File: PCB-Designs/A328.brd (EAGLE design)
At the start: 35.2 x 39.4 mm, 15 parts

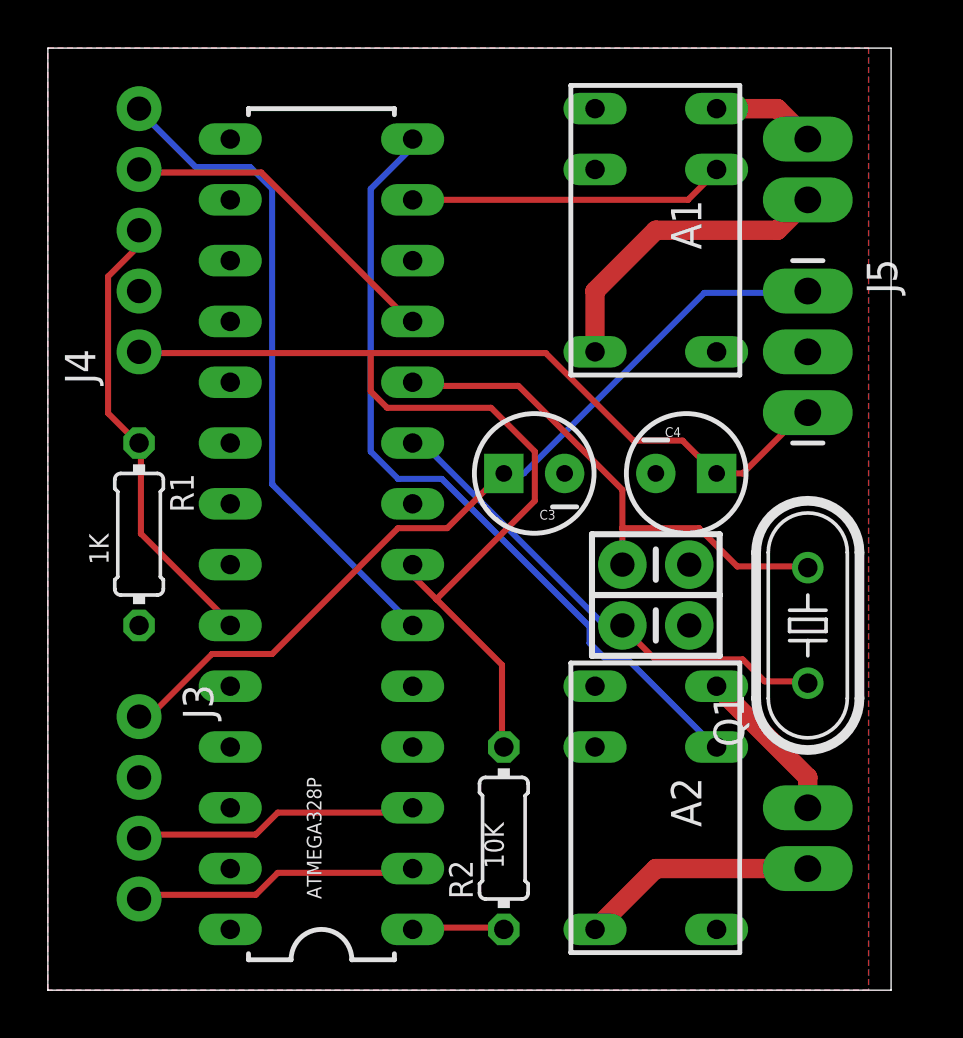
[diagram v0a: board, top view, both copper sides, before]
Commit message: Smaller board, redundant power according to arduino schematic.
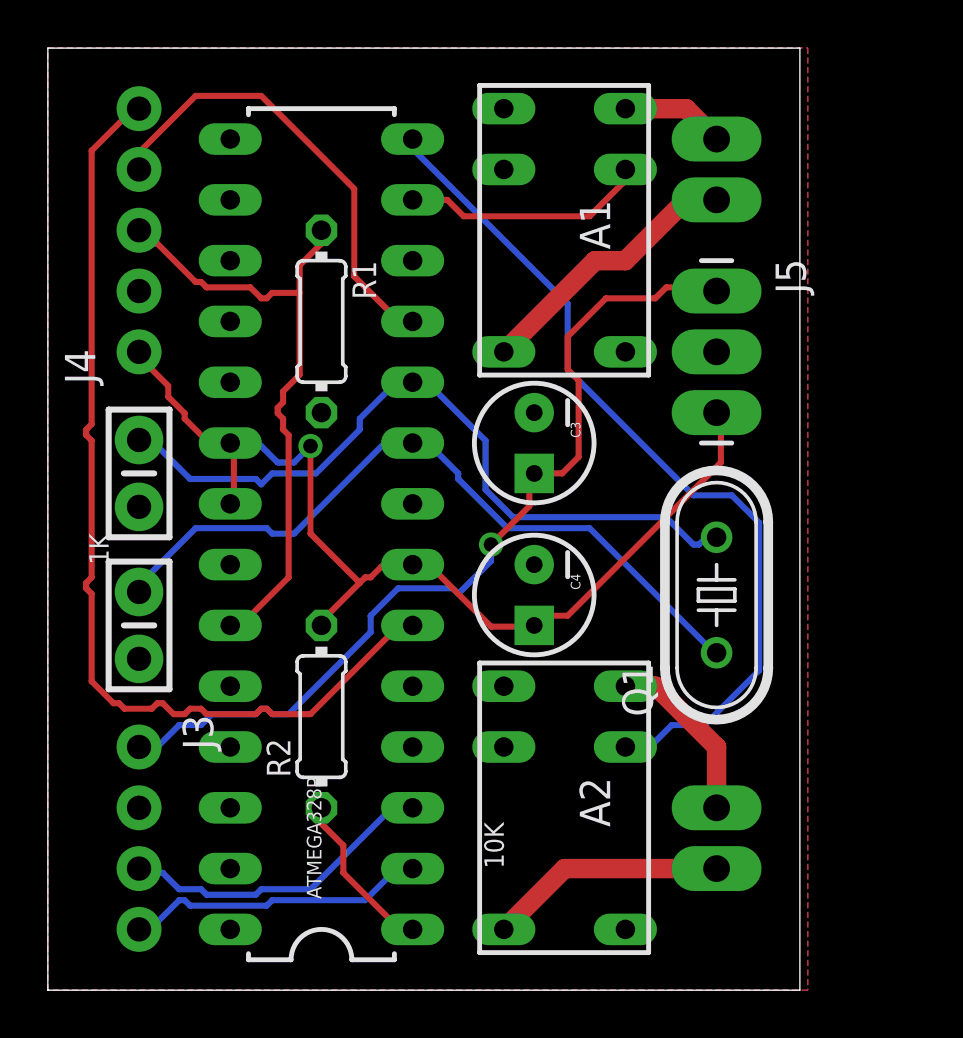
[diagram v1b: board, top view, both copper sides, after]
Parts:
- moved C1 21.9 mm to (3.81, 22.9), turned to 270 degrees
- moved C2 21.6 mm to (3.81, 16.5), turned to 270 degrees
- moved R1 11.7 mm to (11.4, 29.2)
- moved R2 9.16 mm to (11.4, 12.7)
- moved C4 8.13 mm to (20.3, 17.8), turned to 270 degrees
- moved Q1 4.02 mm to (27.9, 17.8)
- moved A1 3.81 mm to (21.6, 33.0)
- moved A2 3.81 mm to (21.6, 8.89)
- moved J1 3.81 mm to (27.9, 34.3)
- moved J2 3.81 mm to (27.9, 6.35)
- moved J5 3.81 mm to (27.9, 30.5)
- moved C3 1.27 mm to (20.3, 24.1), turned to 270 degrees
- moved J3 1.27 mm to (3.81, 11.4)
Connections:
- net +5V: now also ATMEGA328P.20, ATMEGA328P.21
- net GND: now also ATMEGA328P.8
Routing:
- net +5V: track 57.7 -> 43.4 mm, vias 0 -> 1
- net RED: track 27.6 -> 41.4 mm
- net OSC1: track 20.8 -> 31.0 mm
- net OSC2: track 22.2 -> 31.1 mm
- net ABTN: track 19.2 -> 26.7 mm
- net GREEN: track 14.1 -> 19.1 mm
- net RESET: track 3.87 -> 6.96 mm
- net A1: track 13.3 -> 10.3 mm
- net +12V: track 35.3 -> 37.8 mm, vias 0 -> 1
- net A2: track 33.8 -> 36.1 mm
- net A1O: track 13.0 -> 11.5 mm
- net TX: track 12.0 -> 13.4 mm
- net A2I: track 6.66 -> 7.40 mm
- net RX: track 12.0 -> 12.7 mm
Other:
- board size 35.2 x 39.4 mm -> 31.4 x 39.4 mm
